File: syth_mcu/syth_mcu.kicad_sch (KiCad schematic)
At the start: 33 parts, among them J1 USB_C_Receptacle_PowerOnly_6P, J2 Conn_01x05, J3 Conn_01x05, SW1 SW_Push, SW2 SW_Push, SW3 SW_Push, SW4 SW_Push, SW5 SW_Push, U1 TFT_320x240, U2 YAAJ_WeAct_BlackPill_Part_Like, U3 74HC4051, U4 AMS1117-3.3, U5 AMS1117-3.3

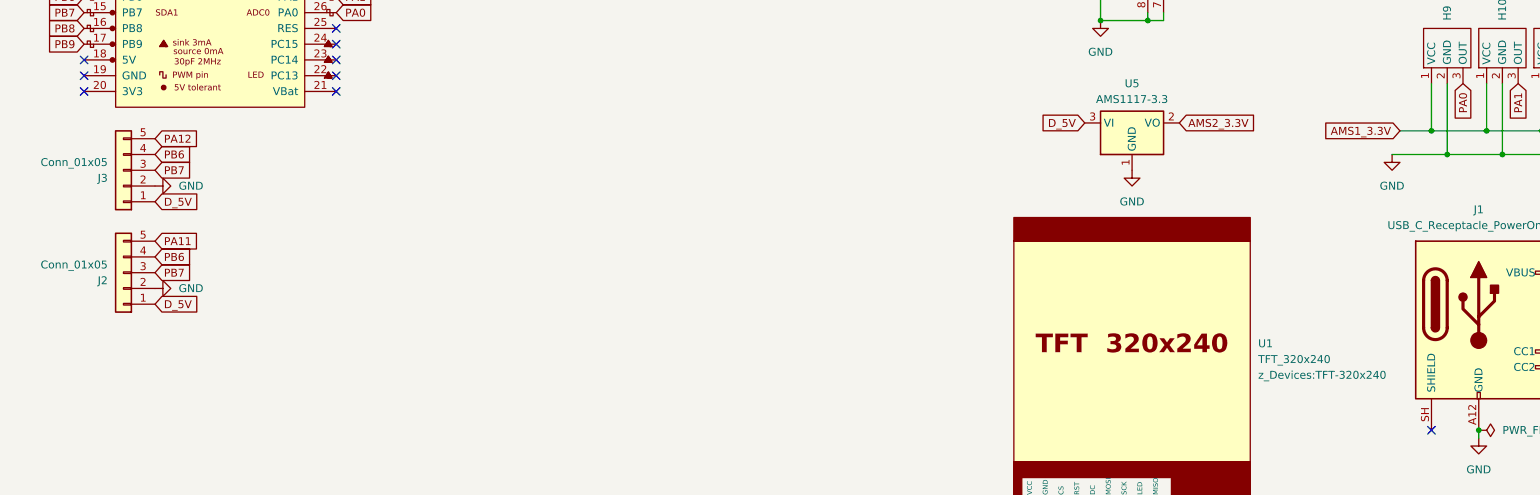
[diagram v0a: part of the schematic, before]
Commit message: kicad: add magnetic pogo connectors, fix footprint/pin mismatches
- add SAMZO PR5L2820-4P-C-F (4P) and PR5L4015-5P-C-F (5P) magnetic
  pogo symbols+footprints, pulled via easyeda2kicad from LCSC
  C41361286 / C41361292
- J2/J3 module links: 5 signals (5V, GND, PB6, PB7, PA11/PA12) need
  the 5-pin pogo footprint, not the 4-pin one
- U2 Black Pill: reassign footprint to YAAJ_WeAct_BlackPill_2
  (40 pads) — YAAJ_BlackPill_1/2 only have 34, missing pins 35-40
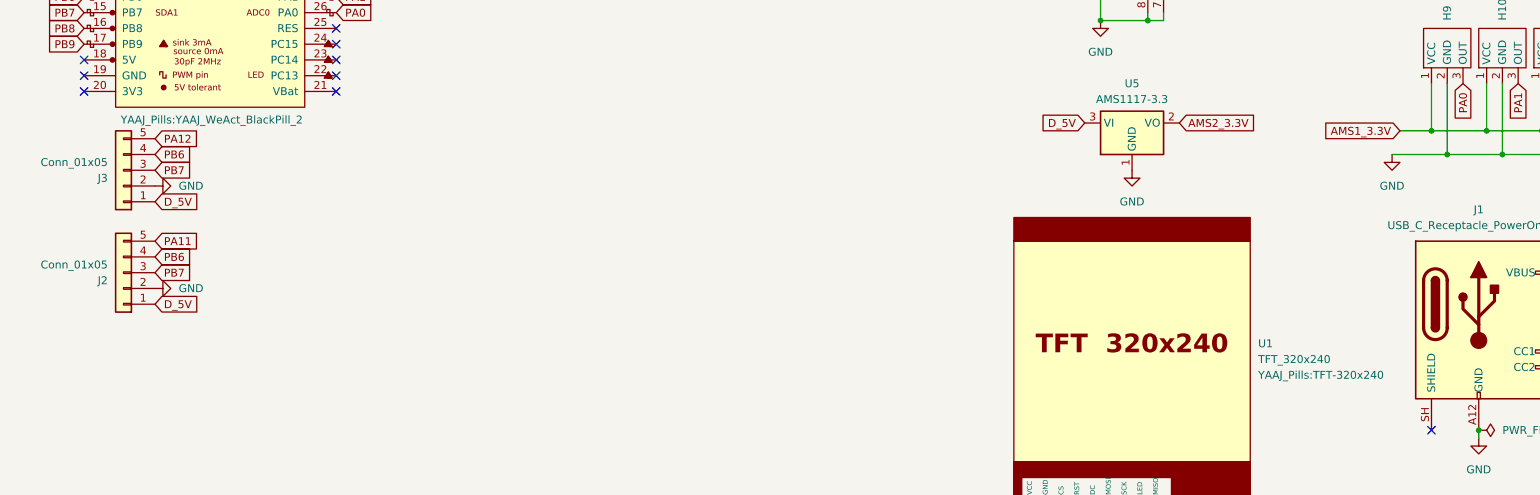
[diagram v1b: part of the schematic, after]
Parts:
- J1: footprint (none) -> Connector_USB:USB_C_Receptacle_Amphenol_12401610E4-2A
- J2, J3: footprint (none) -> synth:CONN-TH_PR5L4015-5P-C-F
- R3, R4: footprint (none) -> Resistor_THT:R_Axial_DIN0207_L6.3mm_D2.5mm_P10.16mm_Horizontal
- RV1, RV2, RV3, RV4, RV5: footprint (none) -> Potentiometer_THT:Potentiometer_Alps_RK09K_Single_Vertical
- SW1, SW2, SW3, SW4, SW5: footprint (none) -> Button_Switch_THT:SW_PUSH_6mm
- U1: footprint z_Devices:TFT-320x240 -> YAAJ_Pills:TFT-320x240
- U2: footprint Kicad-STM32:YAAJ_WeAct_BlackPill2 -> YAAJ_Pills:YAAJ_WeAct_BlackPill_2
- U3: footprint (none) -> Package_DIP:DIP-16_W7.62mm
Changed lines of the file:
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@@
 			)
 		)
-		(property "Footprint" ""
+		(property "Footprint" "synth:CONN-TH_PR5L4015-5P-C-F"
 			(at 31.75 90.17 0)
 			(hide yes)
@@
 			)
 		)
-		(property "Footprint" ""
+		(property "Footprint" "Connector_USB:USB_C_Receptacle_Amphenol_12401610E4-2A"
 			(at 254 111.76 0)
 			(hide yes)
@@
 			)
 		)
-		(property "Footprint" ""
+		(property "Footprint" "Resistor_THT:R_Axial_DIN0207_L6.3mm_D2.5mm_P10.16mm_Horizontal"
 			(at 269.24 121.158 90)
 			(hide yes)
@@
 			)
 		)
-		(property "Footprint" "Kicad-STM32:YAAJ_WeAct_BlackPill2"
+		(property "Footprint" "YAAJ_Pills:YAAJ_WeAct_BlackPill_2"
 			(at 45.974 82.042 0)
-			(hide yes)
 			(show_name no)
 			(do_not_autoplace no)
@@
 			)
 		)
-		(property "Footprint" ""
+		(property "Footprint" "Resistor_THT:R_Axial_DIN0207_L6.3mm_D2.5mm_P10.16mm_Horizontal"
 			(at 269.24 123.698 90)
 			(hide yes)
@@
 			)
 		)
-		(property "Footprint" ""
+		(property "Footprint" "Button_Switch_THT:SW_PUSH_6mm"
 			(at 40.64 152.4 0)
 			(hide yes)
@@
 			)
 		)
-		(property "Footprint" ""
+		(property "Footprint" "Package_DIP:DIP-16_W7.62mm"
 			(at 196.85 59.69 0)
 			(hide yes)
@@
 			)
 		)
-		(property "Footprint" ""
+		(property "Footprint" "Button_Switch_THT:SW_PUSH_6mm"
 			(at 69.85 152.4 0)
 			(hide yes)
@@
 			)
 		)
-		(property "Footprint" ""
+		(property "Footprint" "Potentiometer_THT:Potentiometer_Alps_RK09K_Single_Vertical"
 			(at 77.47 177.8 0)
 			(hide yes)
@@
 			)
 		)
-		(property "Footprint" ""
+		(property "Footprint" "Button_Switch_THT:SW_PUSH_6mm"
 			(at 25.4 152.4 0)
 			(hide yes)
@@
 			)
 		)
-		(property "Footprint" ""
+		(property "Footprint" "Potentiometer_THT:Potentiometer_Alps_RK09K_Single_Vertical"
 			(at 95.25 177.8 0)
 			(hide yes)
@@
 			)
 		)
-		(property "Footprint" ""
+		(property "Footprint" "Button_Switch_THT:SW_PUSH_6mm"
 			(at 55.88 152.4 0)
 			(hide yes)
@@
 			)
 		)
-		(property "Footprint" ""
+		(property "Footprint" "Potentiometer_THT:Potentiometer_Alps_RK09K_Single_Vertical"
 			(at 39.37 177.8 0)
 			(hide yes)
@@
 			)
 		)
-		(property "Footprint" ""
+		(property "Footprint" "Potentiometer_THT:Potentiometer_Alps_RK09K_Single_Vertical"
 			(at 20.32 177.8 0)
 			(hide yes)
@@
 			)
 		)
-		(property "Footprint" ""
+		(property "Footprint" "Button_Switch_THT:SW_PUSH_6mm"
 			(at 83.82 152.4 0)
 			(hide yes)
@@
 	)
 	(symbol
-		(lib_id "power:GND")
-		(at 180.34 146.05 0)
+		(lib_id "synth:H3503")
+		(at 247.65 78.74 90)
 		(unit 1)
 		(body_style 1)
@@
 		(dnp no)
 		(fields_autoplaced yes)
-		(property "Reference" "#PWR015"
-			(at 180.34 152.4 0)
-			(hide yes)
+		(property "Reference" "H10"
+			(at 253.9999 66.04 0)
 			(show_name no)
 			(do_not_autoplace no)
@@
 					(size 1.27 1.27)
 				)
+				(justify left)
 			)
 		)
-		(property "Value" "GND"
-			(at 180.34 151.13 0)
+		(property "Value" ""
+			(at 247.65 78.74 0)
 			(show_name no)
 			(do_not_autoplace no)
@@
 			)
 		)
-		(property "Footprint" ""
-			(at 180.34 146.05 0)
+		(property "Footprint" "Package_TO_SOT_THT:TO-92_Inline"
+			(at 247.65 78.74 0)
 			(hide yes)
 			(show_name no)
@@
 		)
 		(property "Datasheet" ""
-			(at 180.34 146.05 0)
+			(at 247.65 78.74 0)
 			(hide yes)
 			(show_name no)
@@
 			)
 		)
-		(property "Description" "Power symbol creates a global label with name \"GND\" , ground"
-			(at 180.34 146.05 0)
+		(property "Description" ""
+			(at 247.65 78.74 0)
 			(hide yes)
 			(show_name no)
@@
 			)
 		)
+		(pin "3"
+		)
 		(pin "1"
 		)
+		(pin "2"
+		)
 		(instances
 			(project "syth_mcu"
 				(path "/6f6073ad-48fd-4b64-b32f-c8e9bfc21ddc"
-					(reference "#PWR015")
+					(reference "H10")
 					(unit 1)
 				)
@@
 	)
 	(symbol
-		(lib_id "synth:H3503")
-		(at 247.65 78.74 90)
+		(lib_id "Diode:SS14")
+		(at 269.24 106.68 180)
 		(unit 1)
 		(body_style 1)
@@
 		(dnp no)
 		(fields_autoplaced yes)
-		(property "Reference" "H10"
-			(at 253.9999 66.04 0)
+		(property "Reference" "D1"
+			(at 269.5575 100.33 0)
 			(show_name no)
 			(do_not_autoplace no)
@@
 					(size 1.27 1.27)
 				)
-				(justify left)
 			)
 		)
-		(property "Value" ""
-			(at 247.65 78.74 0)
+		(property "Value" "SS14"
+			(at 269.5575 102.87 0)
 			(show_name no)
 			(do_not_autoplace no)
@@
 			)
 		)
-		(property "Footprint" "Package_TO_SOT_THT:TO-92_Inline"
-			(at 247.65 78.74 0)
+		(property "Footprint" "Diode_SMD:D_SMA"
+			(at 269.24 102.235 0)
 			(hide yes)
 			(show_name no)
@@
 			)
 		)
-		(property "Datasheet" ""
-			(at 247.65 78.74 0)
+		(property "Datasheet" "https://www.vishay.com/docs/88746/ss12.pdf"
+			(at 269.24 106.68 0)
 			(hide yes)
 			(show_name no)
@@
 			)
 		)
-		(property "Description" ""
-			(at 247.65 78.74 0)
+		(property "Description" "40V 1A Schottky Diode, SMA"
+			(at 269.24 106.68 0)
 			(hide yes)
 			(show_name no)
@@
 			)
 		)
-		(pin "3"
+		(pin "2"
 		)
 		(pin "1"
 		)
-		(pin "2"
-		)
 		(instances
 			(project "syth_mcu"
 				(path "/6f6073ad-48fd-4b64-b32f-c8e9bfc21ddc"
-					(reference "H10")
+					(reference "D1")
 					(unit 1)
 				)
@@
 	)
 	(symbol
-		(lib_id "Diode:SS14")
-		(at 269.24 106.68 180)
+		(lib_id "power:GND")
+		(at 180.34 146.05 0)
 		(unit 1)
 		(body_style 1)
@@
 		(dnp no)
 		(fields_autoplaced yes)
-		(property "Reference" "D1"
-			(at 269.5575 100.33 0)
+		(property "Reference" "#PWR029"
+			(at 180.34 152.4 0)
+			(hide yes)
 			(show_name no)
 			(do_not_autoplace no)
@@
 			)
 		)
-		(property "Value" "SS14"
-			(at 269.5575 102.87 0)
+		(property "Value" "GND"
+			(at 180.34 151.13 0)
 			(show_name no)
 			(do_not_autoplace no)
@@
 			)
 		)
-		(property "Footprint" "Diode_SMD:D_SMA"
-			(at 269.24 102.235 0)
+		(property "Footprint" ""
+			(at 180.34 146.05 0)
 			(hide yes)
 			(show_name no)
@@
 			)
 		)
-		(property "Datasheet" "https://www.vishay.com/docs/88746/ss12.pdf"
-			(at 269.24 106.68 0)
+		(property "Datasheet" ""
+			(at 180.34 146.05 0)
 			(hide yes)
 			(show_name no)
@@
 			)
 		)
-		(property "Description" "40V 1A Schottky Diode, SMA"
-			(at 269.24 106.68 0)
+		(property "Description" "Power symbol creates a global label with name \"GND\" , ground"
+			(at 180.34 146.05 0)
 			(hide yes)
 			(show_name no)
@@
 			)
 		)
-		(pin "2"
-		)
 		(pin "1"
 		)
@@
 			(project "syth_mcu"
 				(path "/6f6073ad-48fd-4b64-b32f-c8e9bfc21ddc"
-					(reference "D1")
+					(reference "#PWR029")
 					(unit 1)
 				)
@@
 			)
 		)
-		(property "Footprint" ""
+		(property "Footprint" "synth:CONN-TH_PR5L4015-5P-C-F"
 			(at 31.75 106.68 0)
 			(hide yes)
@@
 			)
 		)
-		(property "Footprint" ""
+		(property "Footprint" "Potentiometer_THT:Potentiometer_Alps_RK09K_Single_Vertical"
 			(at 58.42 177.8 0)
 			(hide yes)
@@
 			)
 		)
-		(property "Footprint" "z_Devices:TFT-320x240"
+		(property "Footprint" "YAAJ_Pills:TFT-320x240"
 			(at 214.63 123.1899 0)
 			(show_name no)

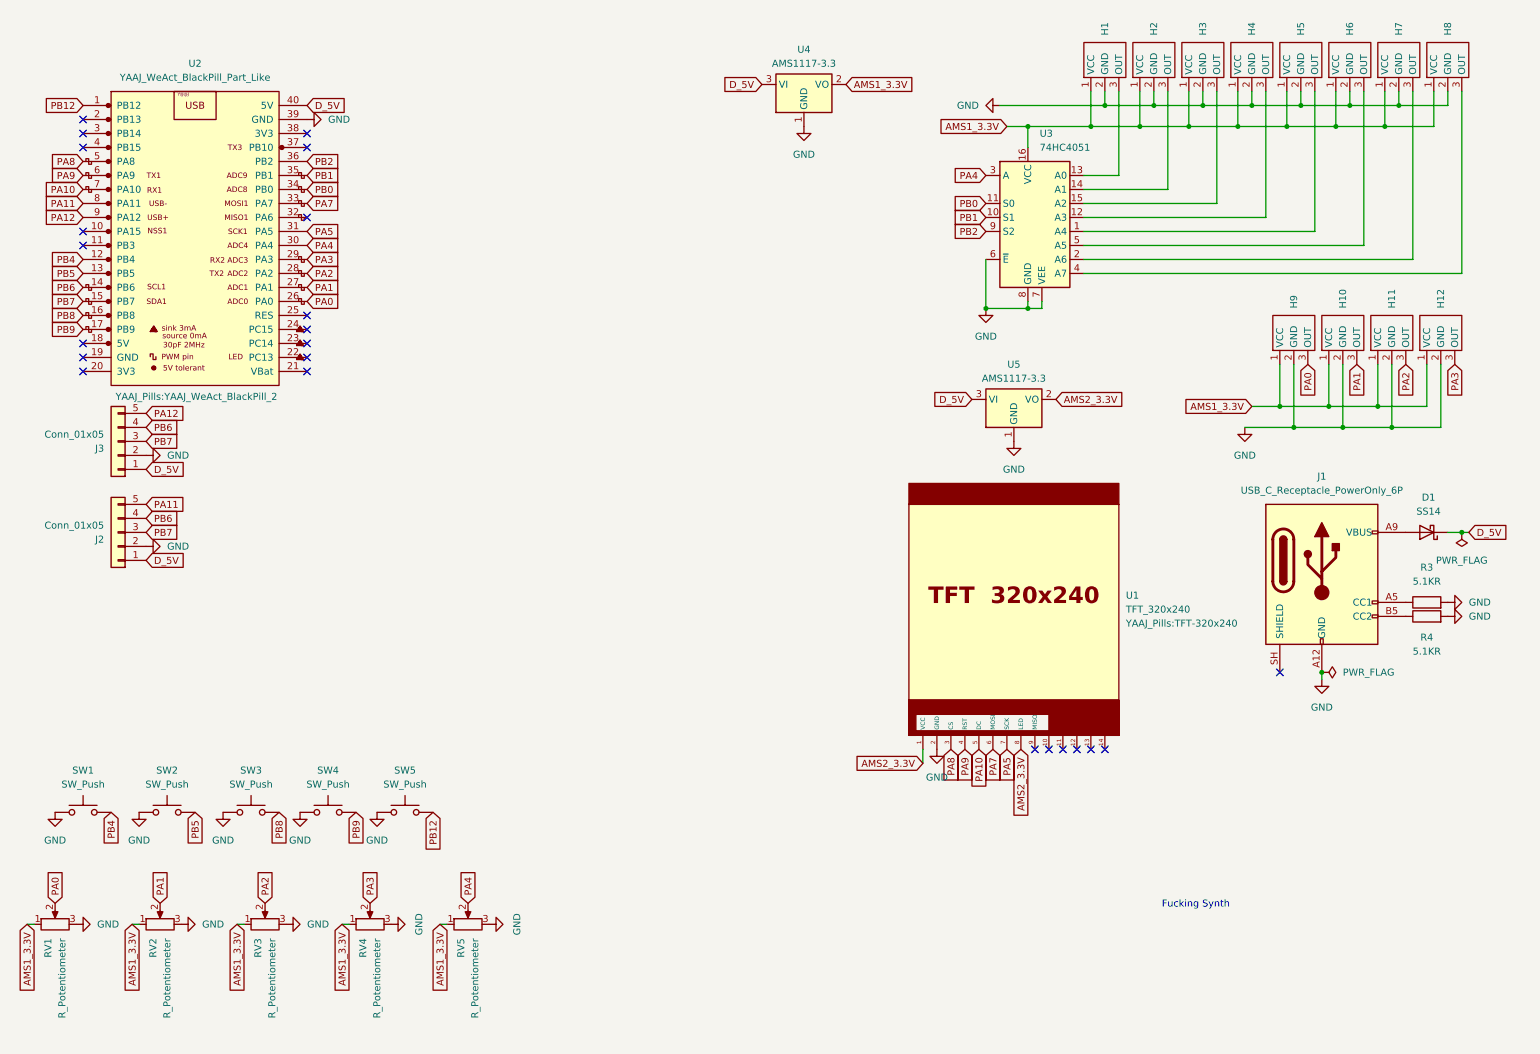
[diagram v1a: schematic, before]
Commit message: kicad: widen board for 12-key hall row, wire DAC power, footprint fixes
- Edge.Cuts resized 167x94.5 -> 286x133mm to fit 12 real-pitch (23mm)
  hall-effect key positions below the control row
- H1-H12 mounting holes shifted to new bottom edge
- add dac-pchannel.kicad_sch as tracked sheet file (was external ref)
- C1/C2 footprint corrected to non-polarized box-film C_Rect
- misc footprint/placement fixes from Cream Bun review pass
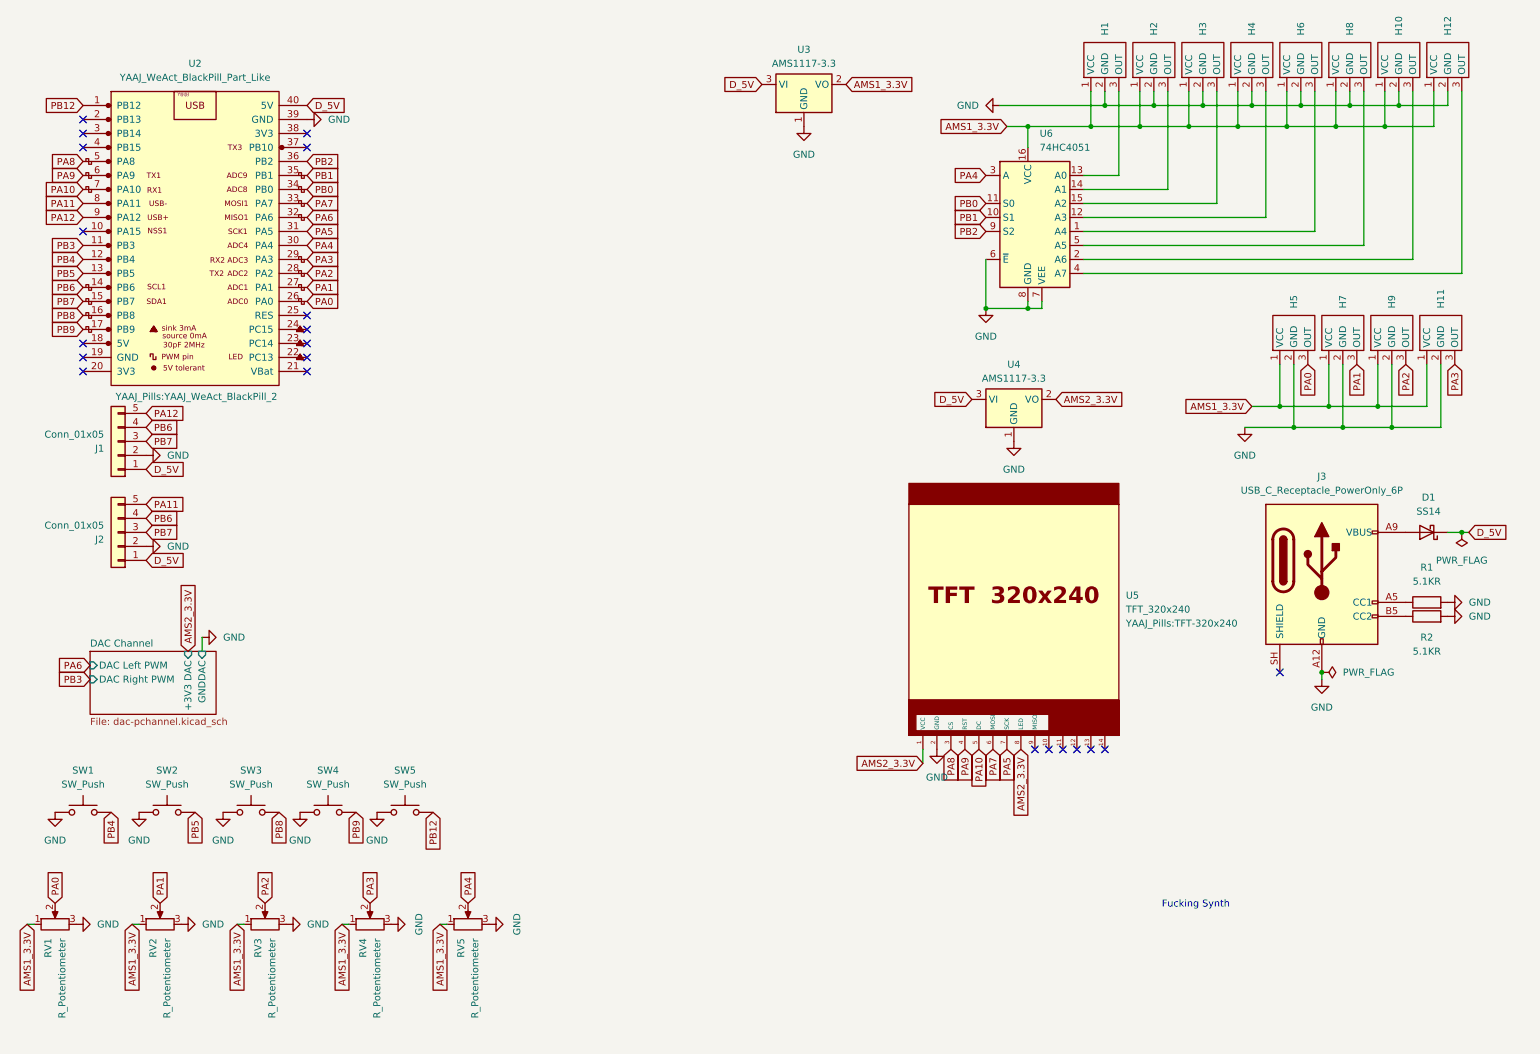
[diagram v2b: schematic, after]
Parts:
- renumbered H7 to H10, H12 to H11, H8 to H12, H9 to H5, H5 to H6, H10 to H7, H6 to H8, H11 to H9, J3 to J1, J1 to J3, R3 to R1, R4 to R2, U4 to U3, U5 to U4, U1 to U5, U3 to U6
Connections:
- net PB3: now reaches U2.11 (PB3)
- net PA6: now reaches U2.32 (PA6)
- no-connect marks 23 -> 21
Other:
- added sheet DAC Channel (dac-pchannel.kicad_sch)

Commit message: update layout
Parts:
- removed H1, H2, H3, H4, H5: (no value), Package_TO_SOT_THT:TO-92_Inline, symbol synth:H3503
- removed U6: 74HC4051, Package_DIP:DIP-16_W7.62mm, symbol 74xx:74HC4051
- added J5, J6: Conn_01x20, Connector_PinSocket_2.54mm:PinSocket_1x20_P2.54mm_Vertical, symbol Connector_Generic:Conn_01x20
- added J7: Conn_01x16, Connector_PinSocket_2.54mm:PinSocket_1x16_P2.54mm_Vertical, symbol Connector_Generic:Conn_01x16
- added J8: Conn_01x08, Connector_PinSocket_2.54mm:PinSocket_1x08_P2.54mm_Vertical, symbol Connector_Generic:Conn_01x08
- added J9: Conn_01x07, Connector_PinSocket_2.54mm:PinSocket_1x07_P2.54mm_Vertical, symbol Connector_Generic:Conn_01x07
- added RV8: R_Potentiometer, Potentiometer_THT:Potentiometer_Alps_RK09K_Single_Vertical, symbol Device:R_Potentiometer
- added SW6: SW_Push, Button_Switch_Keyboard:SW_Cherry_MX_1.00u_PCB, symbol Switch:SW_Push
- SW1, SW2, SW3, SW4, SW5: footprint Button_Switch_THT:SW_PUSH_6mm -> Button_Switch_Keyboard:SW_Cherry_MX_1.00u_PCB
- U5: footprint YAAJ_Pills:TFT-320x240 -> Connector_PinHeader_2.54mm:PinHeader_1x14_P2.54mm_Vertical
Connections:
- net AMS1_3.3V: now also H10.2 (GND), H11.2 (GND), H12.2 (GND), H9.2 (GND), J8.7 (Pin_7), J9.6 (Pin_6), RV8.1; no longer H10.1 (VCC), H11.1 (VCC), H12.1 (VCC), H9.1 (VCC)
- net D_5V: now also U2.18 (5V), J5.18 (Pin_18), J6.1 (Pin_1)
- net GND: now also H10.1 (VCC), H11.1 (VCC), H12.1 (VCC), H9.1 (VCC), U2.19 (GND), J5.19 (Pin_19), J6.2 (Pin_2), J8.6 (Pin_6), J8.8 (Pin_8), J9.7 (Pin_7), RV8.3, SW6.1; no longer H10.2 (GND), H11.2 (GND), H12.2 (GND), H9.2 (GND)
- net PA0: now also J6.15 (Pin_15)
- net PA1: now also J6.14 (Pin_14); no longer H7.3 (OUT)
- net PA10: now also J5.7 (Pin_7)
- net PA11: now also J5.8 (Pin_8)
- net PA12: now also J5.9 (Pin_9)
- net PA2: now also J6.13 (Pin_13); no longer H9.3 (OUT)
- net PA3: now also J6.12 (Pin_12); no longer H11.3 (OUT)
- net PA4: now also J6.11 (Pin_11)
- net PA5: now also J6.10 (Pin_10)
- net PA6: now also J6.9 (Pin_9)
- net PA7: now also J6.8 (Pin_8)
- net PA8: now also J5.5 (Pin_5)
- net PA9: now also J5.6 (Pin_6)
- net PB0: now also J6.7 (Pin_7), J8.5 (Pin_5)
- net PB1: now also J6.6 (Pin_6), RV8.2
- net PB12: now also J5.1 (Pin_1)
- net PB2: now also J6.5 (Pin_5), J8.4 (Pin_4)
- net PB3: now also J5.11 (Pin_11)
- net PB4: now also J5.12 (Pin_12)
- net PB5: now also J5.13 (Pin_13)
- net PB6: now also J5.14 (Pin_14)
- net PB7: now also J5.15 (Pin_15)
- net PB8: now also J5.16 (Pin_16)
- net PB9: now also J5.17 (Pin_17)
- net PA15: now reaches U2.10 (PA15)
- net PA15: now also J5.10 (Pin_10)
- net PB13: now reaches U2.2 (PB13)
- net PB13: now also J5.2 (Pin_2), J8.3 (Pin_3)
- net 3V3: now reaches U2.20 (3V3)
- net 3V3: now also U2.38 (3V3), J5.20 (Pin_20), J6.3 (Pin_3)
- net VBat: now reaches U2.21 (VBat)
- net VBat: now also J6.20 (Pin_20)
- net PC13: now reaches U2.22 (PC13)
- net PC13: now also J6.19 (Pin_19)
- net PC14: now reaches U2.23 (PC14)
- net PC14: now also J6.18 (Pin_18)
- net PC15: now reaches U2.24 (PC15)
- net PC15: now also J6.17 (Pin_17), SW6.2
- net RES: now reaches U2.25 (RES)
- net RES: now also J6.16 (Pin_16)
- net PB14: now reaches U2.3 (PB14)
- net PB14: now also J5.3 (Pin_3), J8.2 (Pin_2)
- net PB10: now reaches U2.37 (PB10)
- net PB10: now also J6.4 (Pin_4)
- net PB15: now reaches U2.4 (PB15)
- net PB15: now also J5.4 (Pin_4), J8.1 (Pin_1)
- net C9: now reaches H10.3 (OUT)
- net C9: now also J7.10 (Pin_10)
- net C11: now reaches H12.3 (OUT)
- net C11: now also J7.12 (Pin_12)
- net C5: now reaches H6.3 (OUT)
- net C5: now also J7.6 (Pin_6)
- net C7: now reaches H8.3 (OUT)
- net C7: now also J7.8 (Pin_8)
- new net C0: J7.1 (Pin_1), J9.1 (Pin_1)
- new net C1: J7.2 (Pin_2), J9.2 (Pin_2)
- new net C10: H11.3 (OUT), J7.11 (Pin_11)
- new net C12: J7.13 (Pin_13)
- new net C13: J7.14 (Pin_14)
- new net C14: J7.15 (Pin_15)
- new net C15: J7.16 (Pin_16)
- new net C2: J7.3 (Pin_3), J9.3 (Pin_3)
- new net C3: J7.4 (Pin_4), J9.4 (Pin_4)
- new net C4: J7.5 (Pin_5), J9.5 (Pin_5)
- new net C6: H7.3 (OUT), J7.7 (Pin_7)
- new net C8: H9.3 (OUT), J7.9 (Pin_9)
- no-connect marks 21 -> 7
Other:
- moved on the sheet: H10, H11, H12, H6, H7, H8, H9, J1, J2, U3

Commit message: update layout
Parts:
- removed RV8: R_Potentiometer, Potentiometer_THT:Potentiometer_Alps_RK09K_Single_Vertical, symbol Device:R_Potentiometer
- removed SW6: SW_Push, Button_Switch_Keyboard:SW_Cherry_MX_1.00u_PCB, symbol Switch:SW_Push
